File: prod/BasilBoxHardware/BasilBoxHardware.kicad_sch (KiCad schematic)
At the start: 0 parts

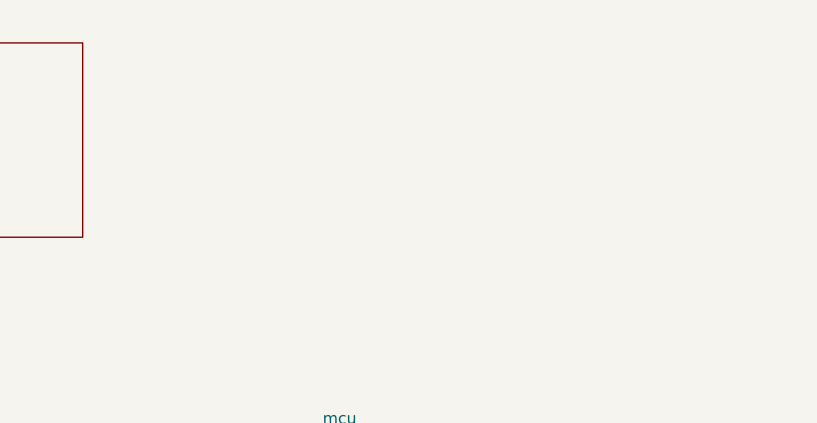
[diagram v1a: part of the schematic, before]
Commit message: Add led light control
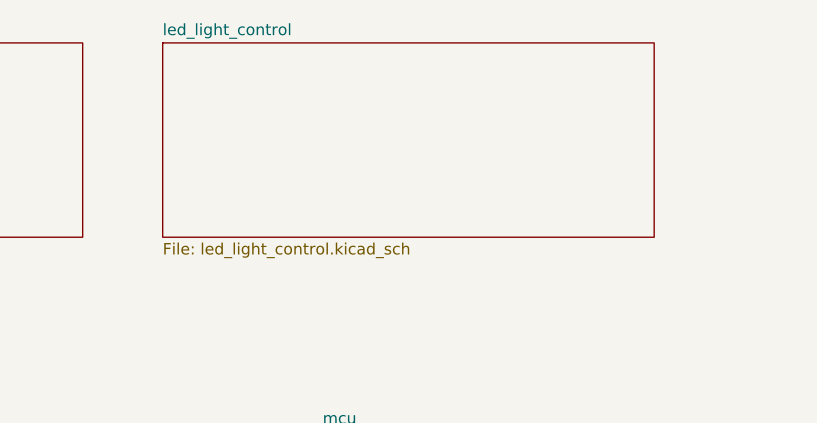
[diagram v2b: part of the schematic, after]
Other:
- added sheet led_light_control (led_light_control.kicad_sch)
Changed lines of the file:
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@@
+    )
+  )
+  (sheet (at 87.63 25.4) (size 54.61 21.59) (fields_autoplaced)
+    (stroke (width 0.1524) (type solid) (color 0 0 0 0))
+    (fill (color 0 0 0 0.0000))
+    (property "Sheet name" "led_light_control" (id 0) (at 87.63 24.6884 0)
+      (effects (font (size 1.27 1.27)) (justify left bottom))
+    )
+    (property "Sheet file" "led_light_control.kicad_sch" (id 1) (at 87.63 47.5746 0)
+      (effects (font (size 1.27 1.27)) (justify left top))
     )
   )
@@
     (path "/de8a0f80-4694-4215-a4c7-c16e58e1df35" (page "2"))
     (path "/3532dee9-6e3a-45a8-875d-a70e3d243b65" (page "3"))
+    (path "/cbb2e553-9a84-4a8e-b29e-b27d4b1bded5" (page "4"))
   )
   (symbol_instances
@@
     )
     (path "/de8a0f80-4694-4215-a4c7-c16e58e1df35/5b6f794a-46eb-4f43-bd8a-950ae1fcf440"
+      (reference "#PWR?") (unit 1) (value "GND") (footprint "")
+    )
+    (path "/cbb2e553-9a84-4a8e-b29e-b27d4b1bded5/5ca767fe-178d-4bd1-9a62-3311f61d1ae1"
       (reference "#PWR?") (unit 1) (value "GND") (footprint "")
     )
@@
       (reference "#PWR?") (unit 1) (value "+3.3V") (footprint "")
     )
+    (path "/cbb2e553-9a84-4a8e-b29e-b27d4b1bded5/df0db37c-671d-4951-9bb8-c8720b5d2fa0"
+      (reference "#PWR?") (unit 1) (value "GND") (footprint "")
+    )
+    (path "/cbb2e553-9a84-4a8e-b29e-b27d4b1bded5/e662d46e-cffe-4f33-ad52-44bb9b3a93f0"
+      (reference "#PWR?") (unit 1) (value "GND") (footprint "")
+    )
     (path "/de8a0f80-4694-4215-a4c7-c16e58e1df35/f3b5e02f-6d92-481a-bdce-402ac6e26a30"
       (reference "#PWR?") (unit 1) (value "+3.3V") (footprint "")
@@
       (reference "U3") (unit 1) (value "DEBO_Relais") (footprint "")
     )
+    (path "/cbb2e553-9a84-4a8e-b29e-b27d4b1bded5/bfe2e29b-66a8-4293-90aa-30815a841c98"
+      (reference "U4") (unit 1) (value "DEBO_Mosfet") (footprint "")
+    )
     (path "/3532dee9-6e3a-45a8-875d-a70e3d243b65/ced067df-3e90-48f8-99c9-9b05a140c33a"
       (reference "U4") (unit 1) (value "FAN") (footprint "")
     )
+    (path "/cbb2e553-9a84-4a8e-b29e-b27d4b1bded5/078d5574-5938-4d85-bad2-574ef53a191f"
+      (reference "U5") (unit 1) (value "LED_LIGHT") (footprint "")
+    )
   )

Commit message: Add hardware schematics
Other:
- added sheet sd_card (sd_card.kicad_sch)
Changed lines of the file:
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@@
     (title "BasilBox")
+  )
+  (sheet (at 152.4 25.4) (size 59.69 21.59) (fields_autoplaced)
+    (stroke (width 0.1524) (type solid) (color 0 0 0 0))
+    (fill (color 0 0 0 0.0000))
+    (property "Sheet name" "sd_card" (id 0) (at 152.4 24.6884 0)
+      (effects (font (size 1.27 1.27)) (justify left bottom))
+    )
+    (property "Sheet file" "sd_card.kicad_sch" (id 1) (at 152.4 47.5746 0)
+      (effects (font (size 1.27 1.27)) (justify left top))
+    )
   )
   (sheet (at 24.13 25.4) (size 54.61 21.59) (fields_autoplaced)
@@
     (path "/3532dee9-6e3a-45a8-875d-a70e3d243b65" (page "3"))
     (path "/cbb2e553-9a84-4a8e-b29e-b27d4b1bded5" (page "4"))
+    (path "/19babd50-6c56-4c8a-b536-ffdb1164a3d1" (page "5"))
   )
   (symbol_instances
+    (path "/19babd50-6c56-4c8a-b536-ffdb1164a3d1/0ec3cd0a-9710-424a-9ec8-7847886a3093"
+      (reference "#PWR?") (unit 1) (value "GND") (footprint "")
+    )
     (path "/3532dee9-6e3a-45a8-875d-a70e3d243b65/29ad90c0-6e19-4c94-bc20-d767d22d513c"
       (reference "#PWR?") (unit 1) (value "+5V") (footprint "")
@@
     (path "/cbb2e553-9a84-4a8e-b29e-b27d4b1bded5/5ca767fe-178d-4bd1-9a62-3311f61d1ae1"
       (reference "#PWR?") (unit 1) (value "GND") (footprint "")
+    )
+    (path "/19babd50-6c56-4c8a-b536-ffdb1164a3d1/6057585b-e475-46e1-a83e-9e7c1eb356f5"
+      (reference "#PWR?") (unit 1) (value "+3V3") (footprint "")
     )
     (path "/de8a0f80-4694-4215-a4c7-c16e58e1df35/763480e7-3762-4f16-a047-9f69445027bc"
@@
       (reference "#PWR?") (unit 1) (value "+3.3V") (footprint "")
     )
+    (path "/19babd50-6c56-4c8a-b536-ffdb1164a3d1/d9fc69c3-8f6f-47fa-a8ae-518114134d7e"
+      (reference "#PWR?") (unit 1) (value "+3V3") (footprint "")
+    )
     (path "/cbb2e553-9a84-4a8e-b29e-b27d4b1bded5/df0db37c-671d-4951-9bb8-c8720b5d2fa0"
       (reference "#PWR?") (unit 1) (value "GND") (footprint "")
     )
     (path "/cbb2e553-9a84-4a8e-b29e-b27d4b1bded5/e662d46e-cffe-4f33-ad52-44bb9b3a93f0"
+      (reference "#PWR?") (unit 1) (value "GND") (footprint "")
+    )
+    (path "/19babd50-6c56-4c8a-b536-ffdb1164a3d1/e7177af8-13bf-49fe-b970-9662979eb73a"
       (reference "#PWR?") (unit 1) (value "GND") (footprint "")
     )
@@
       (reference "U5") (unit 1) (value "LED_LIGHT") (footprint "")
     )
+    (path "/19babd50-6c56-4c8a-b536-ffdb1164a3d1/c9739bd7-ae15-4e44-87fa-6097ebdd34a1"
+      (reference "U?") (unit 1) (value "SD_Demo_Board") (footprint "")
+    )
   )
